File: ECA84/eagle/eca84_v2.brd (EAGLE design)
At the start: 223 x 127 mm, 186 parts

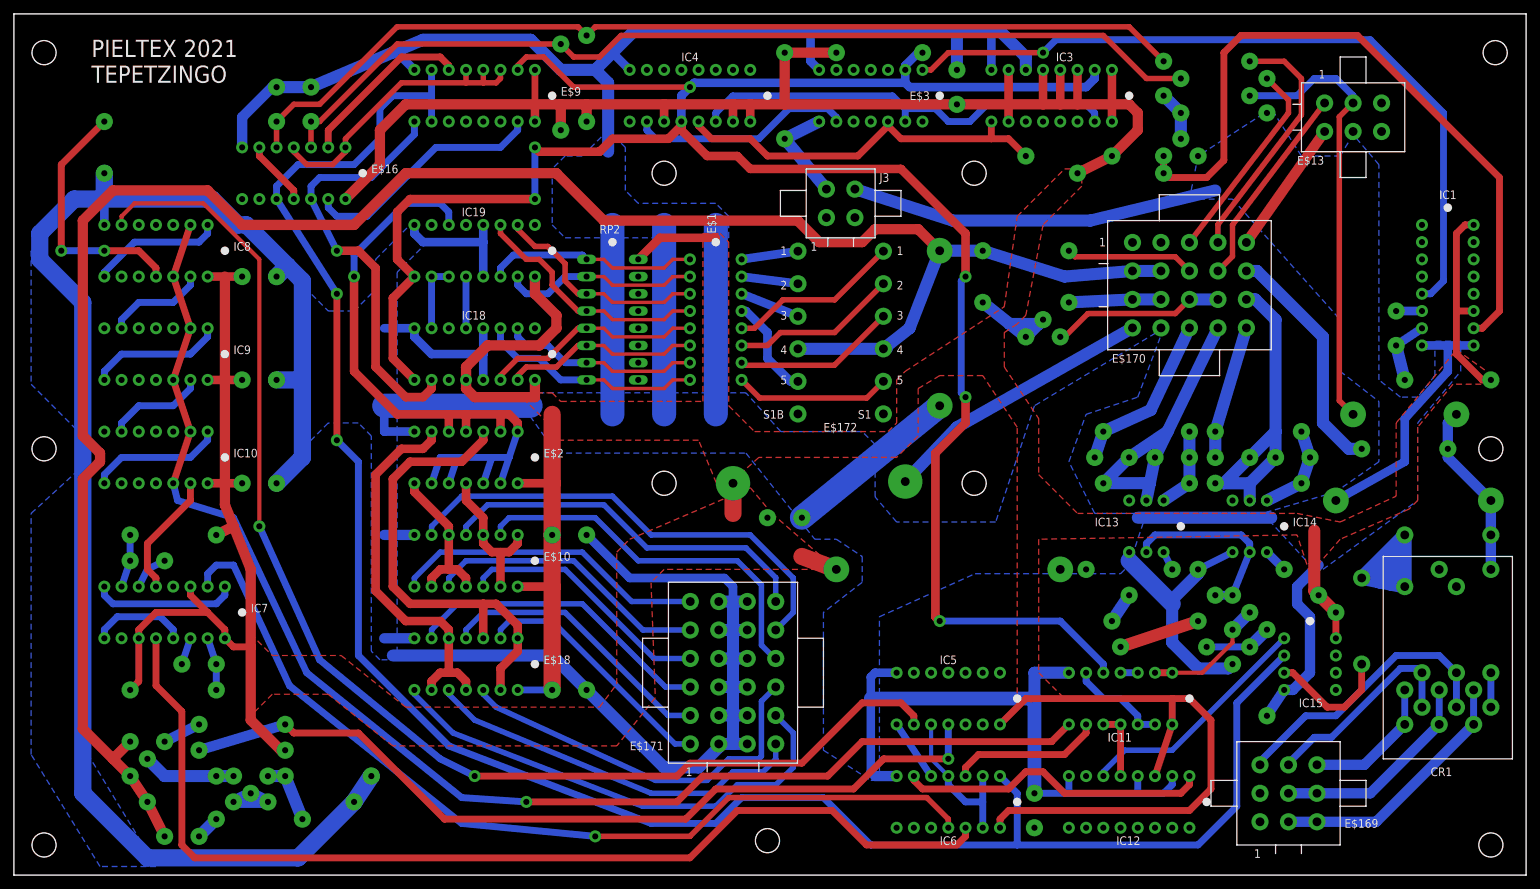
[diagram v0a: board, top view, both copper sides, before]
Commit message: medir pos de orificios
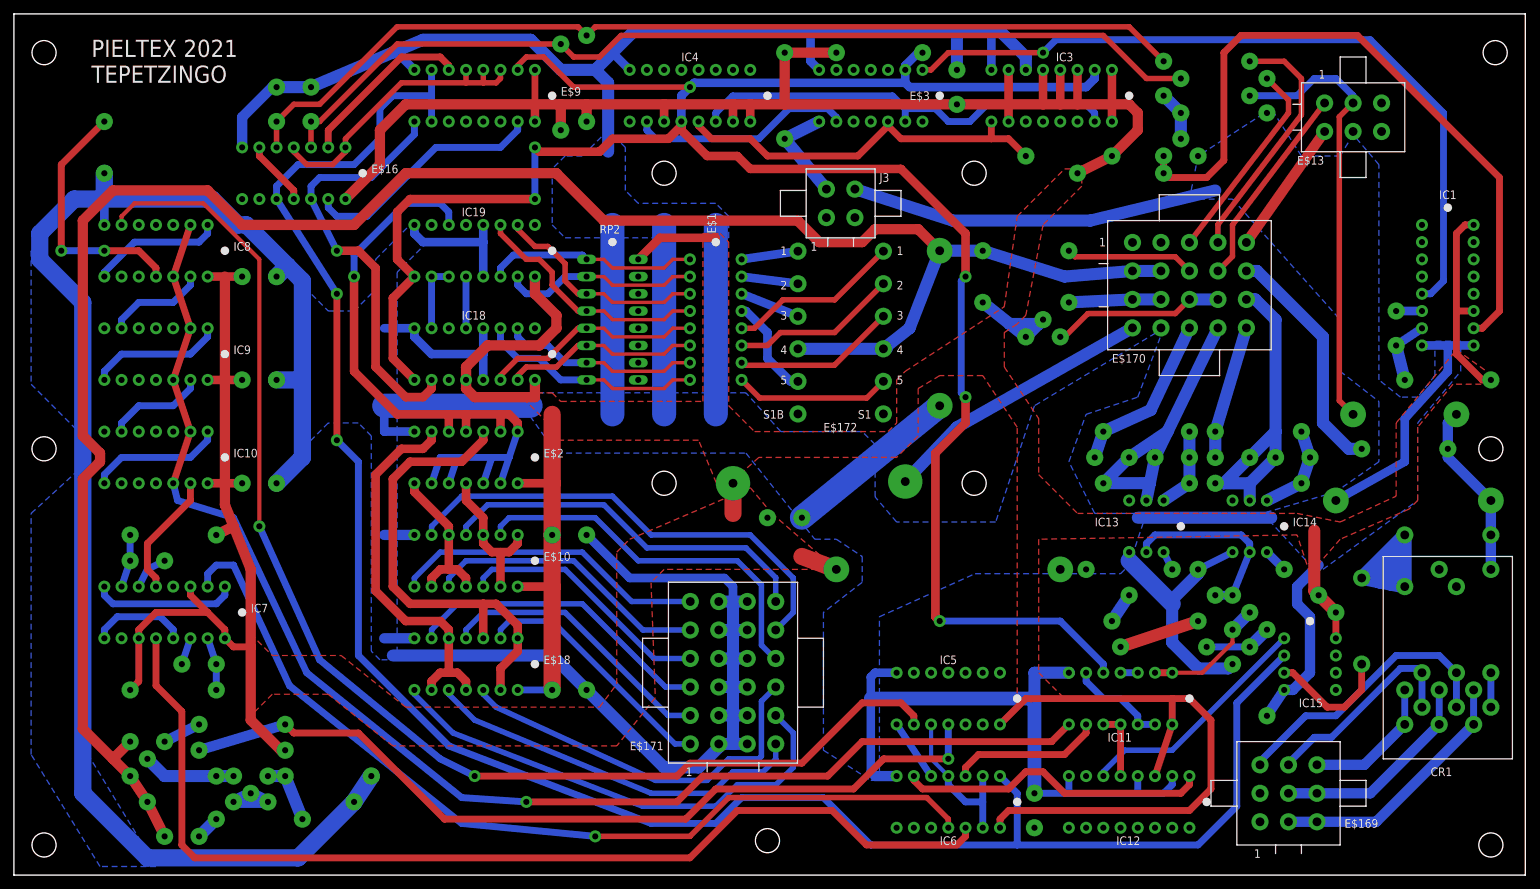
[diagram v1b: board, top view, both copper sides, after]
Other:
- board size 223 x 127 mm -> 222.9 x 127 mm
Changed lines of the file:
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@@
 <grid distance="25" unitdist="mil" unit="mil" style="lines" multiple="1" display="yes" altdistance="5" altunitdist="mil" altunit="mil"/>
 <layers>
-<layer number="1" name="Top" color="4" fill="1" visible="yes" active="yes"/>
+<layer number="1" name="Top" color="4" fill="1" visible="no" active="yes"/>
 <layer number="2" name="Route2" color="16" fill="1" visible="no" active="no"/>
 <layer number="3" name="Route3" color="17" fill="1" visible="no" active="no"/>
@@
 <layer number="14" name="Route14" color="22" fill="1" visible="no" active="no"/>
 <layer number="15" name="Route15" color="23" fill="1" visible="no" active="no"/>
-<layer number="16" name="Bottom" color="1" fill="1" visible="yes" active="yes"/>
-<layer number="17" name="Pads" color="2" fill="1" visible="yes" active="yes"/>
+<layer number="16" name="Bottom" color="1" fill="1" visible="no" active="yes"/>
+<layer number="17" name="Pads" color="2" fill="1" visible="no" active="yes"/>
 <layer number="18" name="Vias" color="2" fill="1" visible="no" active="yes"/>
 <layer number="19" name="Unrouted" color="6" fill="1" visible="yes" active="yes"/>
 <layer number="20" name="Dimension" color="24" fill="1" visible="yes" active="yes"/>
-<layer number="21" name="tPlace" color="7" fill="1" visible="yes" active="yes"/>
+<layer number="21" name="tPlace" color="7" fill="1" visible="no" active="yes"/>
 <layer number="22" name="bPlace" color="7" fill="1" visible="no" active="yes"/>
-<layer number="23" name="tOrigins" color="15" fill="1" visible="yes" active="yes"/>
+<layer number="23" name="tOrigins" color="15" fill="1" visible="no" active="yes"/>
 <layer number="24" name="bOrigins" color="15" fill="1" visible="no" active="yes"/>
-<layer number="25" name="tNames" color="7" fill="1" visible="yes" active="yes"/>
+<layer number="25" name="tNames" color="7" fill="1" visible="no" active="yes"/>
 <layer number="26" name="bNames" color="7" fill="1" visible="no" active="yes"/>
 <layer number="27" name="tValues" color="7" fill="1" visible="yes" active="yes"/>
@@
 <layer number="43" name="vRestrict" color="2" fill="10" visible="no" active="yes"/>
 <layer number="44" name="Drills" color="7" fill="1" visible="no" active="yes"/>
-<layer number="45" name="Holes" color="7" fill="1" visible="no" active="yes"/>
+<layer number="45" name="Holes" color="7" fill="1" visible="yes" active="yes"/>
 <layer number="46" name="Milling" color="3" fill="1" visible="no" active="yes"/>
 <layer number="47" name="Measures" color="7" fill="1" visible="no" active="yes"/>
@@
 <layer number="100" name="topRef" color="22" fill="1" visible="no" active="yes"/>
 <layer number="101" name="bottomRef" color="3" fill="1" visible="no" active="yes"/>
-<layer number="102" name="holeRef" color="23" fill="1" visible="no" active="yes"/>
+<layer number="102" name="holeRef" color="23" fill="1" visible="yes" active="yes"/>
 <layer number="103" name="viaRef" color="10" fill="1" visible="no" active="yes"/>
 </layers>
 <board>
 <plain>
-<wire x1="0" y1="127" x2="223" y2="127" width="0.1" layer="20"/>
-<wire x1="223" y1="127" x2="223" y2="0.000009375" width="0.1" layer="20"/>
-<wire x1="223" y1="0.000009375" x2="0" y2="0.000009375" width="0.1" layer="20"/>
-<wire x1="0" y1="0.000009375" x2="0" y2="127" width="0.1" layer="20"/>
+<wire x1="0" y1="127" x2="222.885" y2="127" width="0.1" layer="20"/>
+<wire x1="222.885" y1="127" x2="222.885" y2="0" width="0.1" layer="20"/>
+<wire x1="222.885" y1="0" x2="0" y2="0" width="0.1" layer="20"/>
+<wire x1="0" y1="0" x2="0" y2="127" width="0.1" layer="20"/>
 <wire x1="173.162" y1="86.0664" x2="172.6" y2="85.8245" width="0.1" layer="101"/>
 <wire x1="172.6" y1="85.8245" x2="172.373" y2="85.2559" width="0.1" layer="101"/>
@@
 <text x="11.43" y="116.84" size="2.54" layer="25">PIELTEX 2021
 TEPETZINGO</text>
+<dimension x1="-0.635" y1="127" x2="-0.635" y2="121.285" x3="-0.635" y3="124.1425" textsize="1.778" layer="20"/>
+<dimension x1="-1.905" y1="121.285" x2="-1.905" y2="62.865" x3="-1.905" y3="92.075" textsize="1.778" layer="20"/>
+<dimension x1="-0.635" y1="0" x2="-0.635" y2="4.445" x3="-0.635" y3="2.2225" textsize="1.778" layer="20"/>
+<dimension x1="-3.81" y1="5.08" x2="-3.81" y2="62.865" x3="-3.81" y3="33.9725" textsize="1.778" layer="20"/>
+<dimension x1="9.525" y1="127" x2="9.525" y2="62.865" x3="9.525" y3="94.9325" textsize="1.778" layer="20"/>
+<dimension x1="9.525" y1="62.865" x2="9.525" y2="0" x3="9.525" y3="31.4325" textsize="1.778" layer="20"/>
+<dimension x1="0" y1="127.635" x2="4.445" y2="127.635" x3="2.2225" y3="127.635" textsize="1.778" layer="20"/>
+<dimension x1="0" y1="-3.175" x2="4.445" y2="-3.175" x3="2.2225" y3="-3.175" textsize="1.778" layer="20"/>
+<dimension x1="95.885" y1="106.045" x2="0" y2="106.045" x3="47.9425" y3="106.045" textsize="1.778" layer="20"/>
+<dimension x1="92.71" y1="103.505" x2="92.71" y2="127" x3="92.71" y3="115.2525" textsize="1.778" layer="20"/>
+<dimension x1="95.885" y1="106.045" x2="141.605" y2="106.045" x3="118.745" y3="106.045" textsize="1.778" layer="20"/>
+<dimension x1="141.605" y1="106.045" x2="222.885" y2="106.045" x3="182.245" y3="106.045" textsize="1.778" layer="20"/>
+<dimension x1="92.71" y1="103.505" x2="92.71" y2="57.785" x3="92.71" y3="80.645" textsize="1.778" layer="20"/>
+<dimension x1="95.885" y1="55.245" x2="0" y2="55.245" x3="47.9425" y3="55.245" textsize="1.778" layer="20"/>
+<dimension x1="95.885" y1="55.245" x2="141.605" y2="55.245" x3="118.745" y3="55.245" textsize="1.778" layer="20"/>
+<dimension x1="141.605" y1="55.245" x2="222.885" y2="55.245" x3="182.245" y3="55.245" textsize="1.778" layer="20"/>
+<dimension x1="92.71" y1="57.785" x2="92.71" y2="0" x3="92.71" y3="28.8925" textsize="1.778" layer="20"/>
+<dimension x1="114.3" y1="5.08" x2="114.3" y2="0" x3="114.3" y3="2.54" textsize="1.778" layer="20"/>
+<dimension x1="144.78" y1="103.505" x2="144.78" y2="127" x3="144.78" y3="115.2525" textsize="1.778" layer="20"/>
+<dimension x1="144.78" y1="103.505" x2="144.78" y2="57.785" x3="144.78" y3="80.645" textsize="1.778" layer="20"/>
+<dimension x1="144.78" y1="57.785" x2="144.78" y2="0" x3="144.78" y3="28.8925" textsize="1.778" layer="20"/>
+<dimension x1="111.125" y1="-3.81" x2="222.885" y2="-3.81" x3="167.005" y3="-3.81" textsize="1.778" layer="20"/>
+<dimension x1="111.125" y1="-3.81" x2="0" y2="-3.81" x3="55.5625" y3="-3.81" textsize="1.778" layer="20"/>
+<dimension x1="217.805" y1="-1.27" x2="222.885" y2="-1.27" x3="220.345" y3="-1.27" textsize="1.778" layer="20"/>
+<dimension x1="224.155" y1="0" x2="224.155" y2="4.445" x3="224.155" y3="2.2225" textsize="1.778" layer="20"/>
+<dimension x1="225.425" y1="4.445" x2="225.425" y2="62.865" x3="225.425" y3="33.655" textsize="1.778" layer="20"/>
+<dimension x1="225.425" y1="62.865" x2="225.425" y2="121.285" x3="225.425" y3="92.075" textsize="1.778" layer="20"/>
+<dimension x1="225.425" y1="121.285" x2="225.425" y2="127" x3="225.425" y3="124.1425" textsize="1.778" layer="20"/>
+<dimension x1="4.445" y1="59.69" x2="0" y2="59.69" x3="2.2225" y3="59.69" textsize="1.778" layer="20"/>
+<dimension x1="217.805" y1="59.69" x2="222.885" y2="59.69" x3="220.345" y3="59.69" textsize="1.778" layer="20"/>
+<dimension x1="218.44" y1="118.745" x2="222.885" y2="118.745" x3="220.6625" y3="118.745" textsize="1.778" layer="20"/>
+<dimension x1="218.44" y1="128.27" x2="222.885" y2="128.27" x3="220.6625" y3="128.27" textsize="1.778" layer="20"/>
+<dimension x1="213.36" y1="127" x2="213.36" y2="62.865" x3="213.36" y3="94.9325" textsize="1.778" layer="20"/>
+<dimension x1="213.36" y1="62.865" x2="213.36" y2="0" x3="213.36" y3="31.4325" textsize="1.778" layer="20"/>
 </plain>
 <attributes>

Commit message: ajustar orificios y exportar archivos CAM
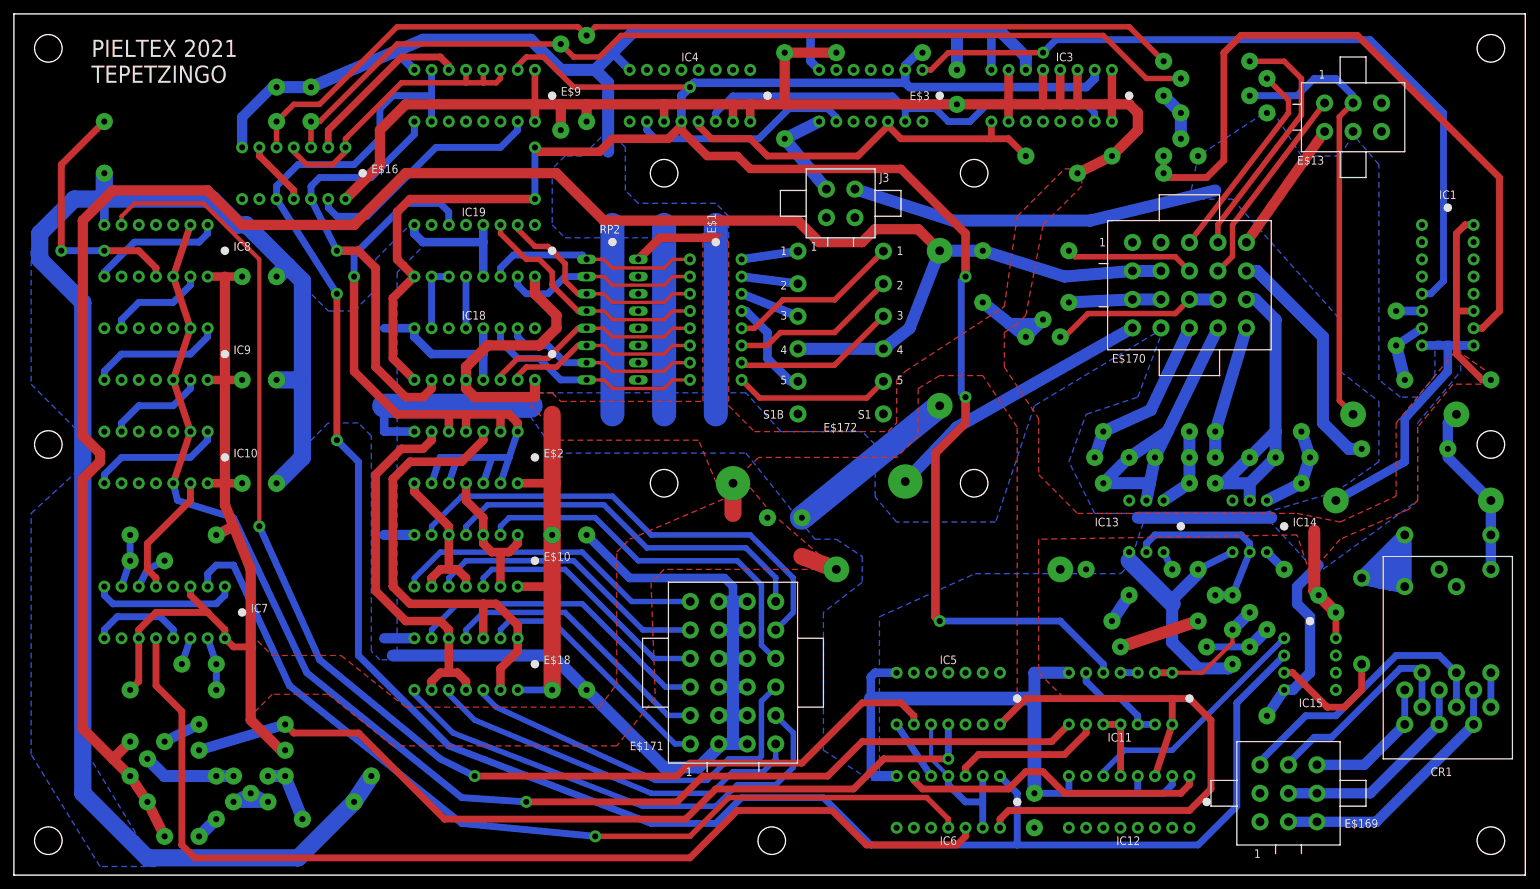
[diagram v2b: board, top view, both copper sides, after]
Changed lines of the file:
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@@
 <layer number="100" name="topRef" color="22" fill="1" visible="no" active="yes"/>
 <layer number="101" name="bottomRef" color="3" fill="1" visible="no" active="yes"/>
-<layer number="102" name="holeRef" color="23" fill="1" visible="yes" active="yes"/>
+<layer number="102" name="holeRef" color="23" fill="1" visible="no" active="yes"/>
 <layer number="103" name="viaRef" color="10" fill="1" visible="no" active="yes"/>
 </layers>
@@
 <wire x1="8.03443125" y1="92.46665" x2="8.00305" y2="92.22388125" width="0.1" layer="103"/>
 <wire x1="8.00305" y1="92.22388125" x2="7.854490625" y2="92.02931875" width="0.1" layer="103"/>
-<hole x="4.445" y="121.285" drill="3.556"/>
-<hole x="4.445" y="62.865" drill="3.556"/>
-<hole x="4.445" y="4.445" drill="3.556"/>
-<hole x="111.125" y="5.08" drill="3.556"/>
-<hole x="95.885" y="57.785" drill="3.556"/>
-<hole x="141.605" y="57.785" drill="3.556"/>
-<hole x="141.605" y="103.505" drill="3.556"/>
-<hole x="95.885" y="103.505" drill="3.556"/>
-<hole x="218.44" y="121.285" drill="3.556"/>
-<hole x="217.805" y="62.865" drill="3.556"/>
-<hole x="217.805" y="4.445" drill="3.556"/>
+<hole x="5.08" y="121.92" drill="4.064"/>
+<hole x="5.08" y="63.5" drill="4.064"/>
+<hole x="5.08" y="5.08" drill="4.064"/>
+<hole x="111.76" y="5.08" drill="4.064"/>
+<hole x="95.885" y="57.785" drill="4.064"/>
+<hole x="141.605" y="57.785" drill="4.064"/>
+<hole x="141.605" y="103.505" drill="4.064"/>
+<hole x="95.885" y="103.505" drill="4.064"/>
+<hole x="217.805" y="121.92" drill="4.064"/>
+<hole x="217.805" y="63.5" drill="4.064"/>
+<hole x="217.805" y="5.08" drill="4.064"/>
 <text x="11.43" y="116.84" size="2.54" layer="25">PIELTEX 2021
 TEPETZINGO</text>
-<dimension x1="-0.635" y1="127" x2="-0.635" y2="121.285" x3="-0.635" y3="124.1425" textsize="1.778" layer="20"/>
-<dimension x1="-1.905" y1="121.285" x2="-1.905" y2="62.865" x3="-1.905" y3="92.075" textsize="1.778" layer="20"/>
-<dimension x1="-0.635" y1="0" x2="-0.635" y2="4.445" x3="-0.635" y3="2.2225" textsize="1.778" layer="20"/>
-<dimension x1="-3.81" y1="5.08" x2="-3.81" y2="62.865" x3="-3.81" y3="33.9725" textsize="1.778" layer="20"/>
+<dimension x1="-0.635" y1="127" x2="-0.635" y2="121.92" x3="-0.635" y3="124.46" textsize="1.778" layer="20"/>
+<dimension x1="-1.905" y1="121.92" x2="-1.905" y2="63.5" x3="-1.905" y3="92.71" textsize="1.778" layer="20"/>
+<dimension x1="-0.635" y1="0" x2="-0.635" y2="5.08" x3="-0.635" y3="2.54" textsize="1.778" layer="20"/>
+<dimension x1="-3.81" y1="5.08" x2="-3.81" y2="63.5" x3="-3.81" y3="34.29" textsize="1.778" layer="20"/>
 <dimension x1="9.525" y1="127" x2="9.525" y2="62.865" x3="9.525" y3="94.9325" textsize="1.778" layer="20"/>
 <dimension x1="9.525" y1="62.865" x2="9.525" y2="0" x3="9.525" y3="31.4325" textsize="1.778" layer="20"/>
-<dimension x1="0" y1="127.635" x2="4.445" y2="127.635" x3="2.2225" y3="127.635" textsize="1.778" layer="20"/>
-<dimension x1="0" y1="-3.175" x2="4.445" y2="-3.175" x3="2.2225" y3="-3.175" textsize="1.778" layer="20"/>
+<dimension x1="0" y1="128.27" x2="5.08" y2="128.27" x3="2.54" y3="128.27" textsize="1.778" layer="20"/>
+<dimension x1="0" y1="-3.175" x2="5.08" y2="-3.175" x3="2.54" y3="-3.175" textsize="1.778" layer="20"/>
 <dimension x1="95.885" y1="106.045" x2="0" y2="106.045" x3="47.9425" y3="106.045" textsize="1.778" layer="20"/>
 <dimension x1="92.71" y1="103.505" x2="92.71" y2="127" x3="92.71" y3="115.2525" textsize="1.778" layer="20"/>
@@
 <dimension x1="111.125" y1="-3.81" x2="0" y2="-3.81" x3="55.5625" y3="-3.81" textsize="1.778" layer="20"/>
 <dimension x1="217.805" y1="-1.27" x2="222.885" y2="-1.27" x3="220.345" y3="-1.27" textsize="1.778" layer="20"/>
-<dimension x1="224.155" y1="0" x2="224.155" y2="4.445" x3="224.155" y3="2.2225" textsize="1.778" layer="20"/>
-<dimension x1="225.425" y1="4.445" x2="225.425" y2="62.865" x3="225.425" y3="33.655" textsize="1.778" layer="20"/>
-<dimension x1="225.425" y1="62.865" x2="225.425" y2="121.285" x3="225.425" y3="92.075" textsize="1.778" layer="20"/>
-<dimension x1="225.425" y1="121.285" x2="225.425" y2="127" x3="225.425" y3="124.1425" textsize="1.778" layer="20"/>
-<dimension x1="4.445" y1="59.69" x2="0" y2="59.69" x3="2.2225" y3="59.69" textsize="1.778" layer="20"/>
+<dimension x1="221.615" y1="0" x2="221.615" y2="5.08" x3="221.615" y3="2.54" textsize="1.778" layer="20"/>
+<dimension x1="225.425" y1="5.08" x2="225.425" y2="63.5" x3="225.425" y3="34.29" textsize="1.778" layer="20"/>
+<dimension x1="225.425" y1="63.5" x2="225.425" y2="121.92" x3="225.425" y3="92.71" textsize="1.778" layer="20"/>
+<dimension x1="221.615" y1="121.92" x2="221.615" y2="127" x3="221.615" y3="124.46" textsize="1.778" layer="20"/>
+<dimension x1="5.08" y1="59.69" x2="0" y2="59.69" x3="2.54" y3="59.69" textsize="1.778" layer="20"/>
 <dimension x1="217.805" y1="59.69" x2="222.885" y2="59.69" x3="220.345" y3="59.69" textsize="1.778" layer="20"/>
 <dimension x1="218.44" y1="118.745" x2="222.885" y2="118.745" x3="220.6625" y3="118.745" textsize="1.778" layer="20"/>
-<dimension x1="218.44" y1="128.27" x2="222.885" y2="128.27" x3="220.6625" y3="128.27" textsize="1.778" layer="20"/>
+<dimension x1="217.805" y1="128.27" x2="222.885" y2="128.27" x3="220.345" y3="128.27" textsize="1.778" layer="20"/>
 <dimension x1="213.36" y1="127" x2="213.36" y2="62.865" x3="213.36" y3="94.9325" textsize="1.778" layer="20"/>
 <dimension x1="213.36" y1="62.865" x2="213.36" y2="0" x3="213.36" y3="31.4325" textsize="1.778" layer="20"/>
